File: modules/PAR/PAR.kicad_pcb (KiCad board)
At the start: 2 copper layers, 160 x 100 mm, 30 parts, among them J1 CardConnector, SW1 SW_DIP_x06, U1 2102, U10 74AHCT541, U11 74HCT32, U12 74AHCT244, U13 74HCT00, U14 74HC688, U15 74AHCT244, U2 2102, U3 2102, U4 2102, U5 2102, U6 2102, U7 2102, U8 2102, U9 74AHCT541

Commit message: serial & cpu card
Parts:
- removed C1, C10, C11, C2, C3, C4, C5, C6, C7, C8: 100n, IMNOTWOPR:C_Rect_P200mil
- removed C9: 47u, IMNOTWOPR:CP_Radial_Tantal_P100mil
- removed RN1: 10k, Resistor_THT:R_Array_SIP7
- removed SW1: SW_DIP_x06, Button_Switch_THT:SW_DIP_SPSTx06_Slide_9.78x17.42mm_W7.62mm_P2.54mm
- removed U1, U2, U3, U4, U5, U6, U7, U8: 2102, IMNOTWOPR:DIP-16N
- removed U10, U9: 74AHCT541, IMNOTWOPR:DIP-20N
- removed U11: 74HCT32, IMNOTWOPR:DIP-14N
- removed U12, U15: 74AHCT244, IMNOTWOPR:DIP-20N
- removed U13: 74HCT00, IMNOTWOPR:DIP-14N
- removed U14: 74HC688, IMNOTWOPR:DIP-20N
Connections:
- J1 pad a10: /RAM-1/SA6 -> /TEMPLATE/S6
- J1 pad a11: /RAM-1/SA7 -> /TEMPLATE/S7
- J1 pad a12: /RAM-1/SA8 -> /TEMPLATE/S8
- J1 pad a13: /RAM-1/SA9 -> /TEMPLATE/S9
- J1 pad a14: /RAM-1/SA10 -> /TEMPLATE/S10
- J1 pad a15: /RAM-1/SA11 -> /TEMPLATE/S11
- J1 pad a16: /RAM-1/SA12 -> /TEMPLATE/S12
- J1 pad a17: /RAM-1/SA13 -> /TEMPLATE/S13
- J1 pad a18: /RAM-1/SA14 -> /TEMPLATE/S14
- J1 pad a19: /RAM-1/SA15 -> /TEMPLATE/S15
- J1 pad a4: /RAM-1/SA0 -> /TEMPLATE/S0
- J1 pad a5: /RAM-1/SA1 -> /TEMPLATE/S1
- J1 pad a6: /RAM-1/SA2 -> /TEMPLATE/S2
- J1 pad a7: /RAM-1/SA3 -> /TEMPLATE/S3
- J1 pad a8: /RAM-1/SA4 -> /TEMPLATE/S4
- J1 pad a9: /RAM-1/SA5 -> /TEMPLATE/S5
- J1 pad b10: /RAM-1/SD6 -> unconnected-(J1B-D_{6}-Padb10)
- J1 pad b11: /RAM-1/SD7 -> unconnected-(J1B-D_{7}-Padb11)
- J1 pad b12: /RAM-1/PHI2 -> unconnected-(J1B-Φ_{2}-Padb12)
- J1 pad b13: /RAM-1/R~{W} -> unconnected-(J1B-R~{W}-Padb13)
- J1 pad b4: /RAM-1/SD0 -> unconnected-(J1B-D_{0}-Padb4)
- J1 pad b5: /RAM-1/SD1 -> unconnected-(J1B-D_{1}-Padb5)
- J1 pad b6: /RAM-1/SD2 -> unconnected-(J1B-D_{2}-Padb6)
- J1 pad b7: /RAM-1/SD3 -> unconnected-(J1B-D_{3}-Padb7)
- J1 pad b8: /RAM-1/SD4 -> unconnected-(J1B-D_{4}-Padb8)
- J1 pad b9: /RAM-1/SD5 -> unconnected-(J1B-D_{5}-Padb9)
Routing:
- net GND: track 200.7 -> 0.00 mm
- net +5V: track 106.8 -> 0.00 mm, vias 1 -> 0
- net /RAM-1/A12: track 86.9 -> 0.00 mm
- net /RAM-1/A11: track 84.3 -> 0.00 mm
- net /RAM-1/A10: track 81.8 -> 0.00 mm
- net /RAM-1/A5: track 81.4 -> 0.00 mm
- net /RAM-1/A6: track 81.4 -> 0.00 mm
- net /RAM-1/A1: track 81.4 -> 0.00 mm
- net /RAM-1/A7: track 81.4 -> 0.00 mm
- net /RAM-1/A9: track 81.4 -> 0.00 mm
- net /RAM-1/A8: track 81.4 -> 0.00 mm
- net /RAM-1/A4: track 81.4 -> 0.00 mm
- net /RAM-1/A3: track 81.4 -> 0.00 mm
- net /RAM-1/A2: track 81.4 -> 0.00 mm
- net /RAM-1/A0: track 81.4 -> 0.00 mm
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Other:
- board text removed: "Mounting holes are optional Keepout areas are for for guide rails"

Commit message: par board & schematic wip
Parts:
- added C1: 47µ, IMNOTWOPR:CP_Radial_Tantal_P100mil, F.Cu at (189.4, 48.6)
- added C10: 100n, IMNOTWOPR:C_Rect_P200mil, F.Cu at (184.3, 53.1)
- added C2: 100n, IMNOTWOPR:C_Rect_P200mil, F.Cu at (157.6, 139.4)
- added C3: 100n, IMNOTWOPR:C_Rect_P200mil, F.Cu at (129.7, 139.4)
- added C4: 100n, IMNOTWOPR:C_Rect_P200mil, F.Cu at (197.0, 53.1)
- added C5: 100n, IMNOTWOPR:C_Rect_P200mil, F.Cu at (197.0, 81.0)
- added C6: 100n, IMNOTWOPR:C_Rect_P200mil, F.Cu at (184.3, 101.3)
- added C7: 100n, IMNOTWOPR:C_Rect_P200mil, F.Cu at (184.3, 73.4)
- added C8: 100n, IMNOTWOPR:C_Rect_P200mil, F.Cu at (147.5, 63.2)
- added C9: 100n, IMNOTWOPR:C_Rect_P200mil, F.Cu at (132.2, 65.8)
- added D1: SB140, Diode_THT:D_DO-41_SOD81_P10.16mm_Horizontal, F.Cu at (181.8, 132.7)
- added D2: SB140, Diode_THT:D_DO-41_SOD81_P10.16mm_Horizontal, F.Cu at (181.8, 136.9)
- added JP1: PORT1A, IMNOTWOPR:Jumper_1x03, F.Cu at (109.4, 51.8)
- added JP2: PORT2A, IMNOTWOPR:Jumper_1x03, F.Cu at (109.4, 100.1)
- added JP3: PORT2B, IMNOTWOPR:Jumper_1x03, F.Cu at (109.4, 133.1)
- added JP4: PORT1B, IMNOTWOPR:Jumper_1x03, F.Cu at (109.4, 84.8)
- added R1: 100R, Resistor_THT:R_Axial_DIN0207_L6.3mm_D2.5mm_P2.54mm_Vertical, F.Cu at (101.8, 60.7)
- added R10: 100R, Resistor_THT:R_Axial_DIN0207_L6.3mm_D2.5mm_P2.54mm_Vertical, F.Cu at (78.9, 58.2)
- added R11: 100R, Resistor_THT:R_Axial_DIN0207_L6.3mm_D2.5mm_P2.54mm_Vertical, F.Cu at (101.8, 109.0)
- added R12: 100R, Resistor_THT:R_Axial_DIN0207_L6.3mm_D2.5mm_P2.54mm_Vertical, F.Cu at (99.2, 106.4)
- added R13: 100R, Resistor_THT:R_Axial_DIN0207_L6.3mm_D2.5mm_P2.54mm_Vertical, F.Cu at (96.7, 109.0)
- added R14: 100R, Resistor_THT:R_Axial_DIN0207_L6.3mm_D2.5mm_P2.54mm_Vertical, F.Cu at (94.1, 106.4)
- added R15: 100R, Resistor_THT:R_Axial_DIN0207_L6.3mm_D2.5mm_P2.54mm_Vertical, F.Cu at (91.6, 109.0)
- added R16: 100R, Resistor_THT:R_Axial_DIN0207_L6.3mm_D2.5mm_P2.54mm_Vertical, F.Cu at (89.0, 106.4)
- added R17: 100R, Resistor_THT:R_Axial_DIN0207_L6.3mm_D2.5mm_P2.54mm_Vertical, F.Cu at (86.5, 109.0)
- added R18: 100R, Resistor_THT:R_Axial_DIN0207_L6.3mm_D2.5mm_P2.54mm_Vertical, F.Cu at (84.0, 106.4)
- added R19: 100R, Resistor_THT:R_Axial_DIN0207_L6.3mm_D2.5mm_P2.54mm_Vertical, F.Cu at (81.4, 109.0)
- added R2: 100R, Resistor_THT:R_Axial_DIN0207_L6.3mm_D2.5mm_P2.54mm_Vertical, F.Cu at (99.2, 58.2)
- added R20: 100R, Resistor_THT:R_Axial_DIN0207_L6.3mm_D2.5mm_P2.54mm_Vertical, F.Cu at (78.9, 106.4)
- added R21: 100R, Resistor_THT:R_Axial_DIN0207_L6.3mm_D2.5mm_P2.54mm_Vertical, F.Cu at (101.8, 129.3)
- added R22: 100R, Resistor_THT:R_Axial_DIN0207_L6.3mm_D2.5mm_P2.54mm_Vertical, F.Cu at (99.2, 131.8)
- added R23: 100R, Resistor_THT:R_Axial_DIN0207_L6.3mm_D2.5mm_P2.54mm_Vertical, F.Cu at (96.7, 129.3)
- added R24: 100R, Resistor_THT:R_Axial_DIN0207_L6.3mm_D2.5mm_P2.54mm_Vertical, F.Cu at (94.1, 131.8)
- added R25: 100R, Resistor_THT:R_Axial_DIN0207_L6.3mm_D2.5mm_P2.54mm_Vertical, F.Cu at (91.6, 129.3)
- added R26: 100R, Resistor_THT:R_Axial_DIN0207_L6.3mm_D2.5mm_P2.54mm_Vertical, F.Cu at (89.0, 131.8)
- added R27: 100R, Resistor_THT:R_Axial_DIN0207_L6.3mm_D2.5mm_P2.54mm_Vertical, F.Cu at (86.5, 129.3)
- added R28: 100R, Resistor_THT:R_Axial_DIN0207_L6.3mm_D2.5mm_P2.54mm_Vertical, F.Cu at (84.0, 131.8)
- added R29: 100R, Resistor_THT:R_Axial_DIN0207_L6.3mm_D2.5mm_P2.54mm_Vertical, F.Cu at (81.4, 129.3)
- added R3: 100R, Resistor_THT:R_Axial_DIN0207_L6.3mm_D2.5mm_P2.54mm_Vertical, F.Cu at (96.7, 60.7)
- added R30: 100R, Resistor_THT:R_Axial_DIN0207_L6.3mm_D2.5mm_P2.54mm_Vertical, F.Cu at (78.9, 131.8)
- added R31: 100R, Resistor_THT:R_Axial_DIN0207_L6.3mm_D2.5mm_P2.54mm_Vertical, F.Cu at (101.8, 81.0)
- added R32: 100R, Resistor_THT:R_Axial_DIN0207_L6.3mm_D2.5mm_P2.54mm_Vertical, F.Cu at (99.2, 83.6)
- added R33: 100R, Resistor_THT:R_Axial_DIN0207_L6.3mm_D2.5mm_P2.54mm_Vertical, F.Cu at (96.7, 81.0)
- added R34: 100R, Resistor_THT:R_Axial_DIN0207_L6.3mm_D2.5mm_P2.54mm_Vertical, F.Cu at (94.1, 83.6)
- added R35: 100R, Resistor_THT:R_Axial_DIN0207_L6.3mm_D2.5mm_P2.54mm_Vertical, F.Cu at (91.6, 81.0)
- added R36: 100R, Resistor_THT:R_Axial_DIN0207_L6.3mm_D2.5mm_P2.54mm_Vertical, F.Cu at (89.0, 83.6)
- added R37: 100R, Resistor_THT:R_Axial_DIN0207_L6.3mm_D2.5mm_P2.54mm_Vertical, F.Cu at (86.5, 81.0)
- added R38: 100R, Resistor_THT:R_Axial_DIN0207_L6.3mm_D2.5mm_P2.54mm_Vertical, F.Cu at (84.0, 83.6)
- added R39: 100R, Resistor_THT:R_Axial_DIN0207_L6.3mm_D2.5mm_P2.54mm_Vertical, F.Cu at (81.4, 81.0)
- added R4: 100R, Resistor_THT:R_Axial_DIN0207_L6.3mm_D2.5mm_P2.54mm_Vertical, F.Cu at (94.1, 58.2)
- added R40: 100R, Resistor_THT:R_Axial_DIN0207_L6.3mm_D2.5mm_P2.54mm_Vertical, F.Cu at (78.9, 83.6)
- added R5: 100R, Resistor_THT:R_Axial_DIN0207_L6.3mm_D2.5mm_P2.54mm_Vertical, F.Cu at (91.6, 60.7)
- added R6: 100R, Resistor_THT:R_Axial_DIN0207_L6.3mm_D2.5mm_P2.54mm_Vertical, F.Cu at (89.0, 58.2)
- added R7: 100R, Resistor_THT:R_Axial_DIN0207_L6.3mm_D2.5mm_P2.54mm_Vertical, F.Cu at (86.5, 60.7)
- added R8: 100R, Resistor_THT:R_Axial_DIN0207_L6.3mm_D2.5mm_P2.54mm_Vertical, F.Cu at (84.0, 58.2)
- added R9: 100R, Resistor_THT:R_Axial_DIN0207_L6.3mm_D2.5mm_P2.54mm_Vertical, F.Cu at (81.4, 60.7)
- added RN1: 10k, Resistor_THT:R_Array_SIP9, F.Cu at (170.3, 60.7)
- added RN2: 10k, Resistor_THT:R_Array_SIP11, F.Cu at (104.3, 54.4)
- added RN3: 10k, Resistor_THT:R_Array_SIP11, F.Cu at (104.3, 102.6)
- added RN4: 10k, Resistor_THT:R_Array_SIP11, F.Cu at (104.3, 135.6)
- added RN5: 10k, Resistor_THT:R_Array_SIP11, F.Cu at (104.3, 87.4)
- added SW1: SW_DIP_x08, Button_Switch_THT:SW_DIP_SPSTx08_Slide_9.78x22.5mm_W7.62mm_P2.54mm, F.Cu at (158.9, 63.2)
- added U1: W65C22, IMNOTWOPR:DIP-40W, F.Cu at (162.7, 112.8)
- added U10: DB-25 VIA, IMNOTWOPR:IDC-Header_2x13_DB-25, F.Cu at (101.8, 69.6)
- added U11: DB-25 VIA, IMNOTWOPR:IDC-Header_2x13_DB-25, F.Cu at (101.8, 117.9)
- added U2: 74HCT30, IMNOTWOPR:DIP-14N, F.Cu at (131.0, 76.0)
- added U3: 74HCT00, IMNOTWOPR:DIP-14N, F.Cu at (183.0, 63.2)
- added U4: 74AHCT541, IMNOTWOPR:DIP-20N, F.Cu at (195.7, 67.1)
- added U5: 74AHCT541, IMNOTWOPR:DIP-20N, F.Cu at (195.7, 95.0)
- added U6: W65C22, IMNOTWOPR:DIP-40W, F.Cu at (134.8, 112.8)
- added U7: 74AHCT245, IMNOTWOPR:DIP-20N, F.Cu at (183.0, 115.3)
- added U8: 74HCT688, IMNOTWOPR:DIP-20N, F.Cu at (183.0, 87.4)
- added U9: 74HCT138, IMNOTWOPR:DIP-16N, F.Cu at (146.2, 74.7)
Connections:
- J1 pad a10: /TEMPLATE/S6 -> Net-(J1A-A_{6})
- J1 pad a11: /TEMPLATE/S7 -> Net-(J1A-A_{7})
- J1 pad a12: /TEMPLATE/S8 -> Net-(J1A-A_{8})
- J1 pad a13: /TEMPLATE/S9 -> Net-(J1A-A_{9})
- J1 pad a14: /TEMPLATE/S10 -> Net-(J1A-A_{10})
- J1 pad a15: /TEMPLATE/S11 -> Net-(J1A-A_{11})
- J1 pad a16: /TEMPLATE/S12 -> Net-(J1A-A_{12})
- J1 pad a17: /TEMPLATE/S13 -> Net-(J1A-A_{13})
- J1 pad a18: /TEMPLATE/S14 -> Net-(J1A-A_{14})
- J1 pad a19: /TEMPLATE/S15 -> Net-(J1A-A_{15})
- J1 pad a4: /TEMPLATE/S0 -> Net-(J1A-A_{0})
- J1 pad a5: /TEMPLATE/S1 -> Net-(J1A-A_{1})
- J1 pad a6: /TEMPLATE/S2 -> Net-(J1A-A_{2})
- J1 pad a7: /TEMPLATE/S3 -> Net-(J1A-A_{3})
- J1 pad a8: /TEMPLATE/S4 -> Net-(J1A-A_{4})
- J1 pad a9: /TEMPLATE/S5 -> Net-(J1A-A_{5})
- J1 pad b22: unconnected-(J1B-~{BUS_ACK}-Padb22) -> Net-(J1B-D_{0})
- J1 pad b23: unconnected-(J1B-~{ABORT}-Padb23) -> Net-(J1B-D_{1})
- J1 pad b24: unconnected-(J1B-SYNC-Padb24) -> Net-(J1B-D_{2})
- J1 pad b25: unconnected-(J1B-VPB-Padb25) -> Net-(J1B-D_{3})
- J1 pad b26: unconnected-(J1B-MLB-Padb26) -> Net-(J1B-D_{4})
- J1 pad b27: unconnected-(J1B-VDA-Padb27) -> Net-(J1B-D_{5})
- J1 pad b28: unconnected-(J1B-VPA-Padb28) -> Net-(J1B-D_{6})
- J1 pad b29: unconnected-(J1B-RESERVED-Padb29) -> Net-(J1B-D_{7})
- J1 pad b4: unconnected-(J1B-D_{0}-Padb4) -> /#VALID
- J1 pad b5: unconnected-(J1B-D_{1}-Padb5) -> /PHI2
- J1 pad b6: unconnected-(J1B-D_{2}-Padb6) -> /R/W
- J1 pad b7: unconnected-(J1B-D_{3}-Padb7) -> /#RESET
- J1 pad b8: unconnected-(J1B-D_{4}-Padb8) -> /#IRQ
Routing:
- net GND: track 0.00 -> 500.6 mm, vias 0 -> 3
- net +5V: track 0.00 -> 427.3 mm, vias 0 -> 4
- net /PORT1_PB7: track 0.00 -> 114.8 mm, vias 0 -> 2
- net /PORT1_PB6: track 0.00 -> 108.5 mm, vias 0 -> 2
- net /PORT1_PA7: track 0.00 -> 102.1 mm, vias 0 -> 2
- net /PORT1_PB5: track 0.00 -> 102.1 mm, vias 0 -> 2
- net /PORT1_PA6: track 0.00 -> 97.0 mm, vias 0 -> 2
- net /PORT1_PB4: track 0.00 -> 95.8 mm, vias 0 -> 2
- net /PORT1_PA5: track 0.00 -> 92.0 mm, vias 0 -> 2
- net /A1: track 0.00 -> 90.3 mm
- net /A2: track 0.00 -> 90.3 mm
- net /PORT1_PB3: track 0.00 -> 89.4 mm, vias 0 -> 2
- net /PORT1_CB2: track 0.00 -> 89.4 mm, vias 0 -> 2
- net /PORT1_PA4: track 0.00 -> 86.9 mm, vias 0 -> 2
- net /PORT1_CB1: track 0.00 -> 83.1 mm, vias 0 -> 2
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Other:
- board text removed: "${TITLE}"

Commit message: bus overhaul and par wip
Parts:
- moved R19 104.2 mm to (-22.7, 58.2)
- moved R29 104.2 mm to (-22.7, 126.8)
- moved R39 104.2 mm to (-22.7, 78.5)
- moved R9 104.2 mm to (-22.7, 106.4)
- moved U1 104.2 mm to (58.6, 110.2)
- moved U2 104.2 mm to (30.6, 110.2)
- moved C1 104.2 mm to (85.2, 46.1)
- moved C3 104.2 mm to (25.6, 136.9)
- moved JP1 104.2 mm to (5.23, 97.5)
- moved JP2 104.2 mm to (5.23, 49.3)
- moved JP3 104.2 mm to (5.23, 130.6)
- moved JP4 104.2 mm to (5.23, 82.3)
- moved R1 104.2 mm to (-2.39, 106.4)
- moved R10 104.2 mm to (-25.2, 103.9)
- moved R11 104.2 mm to (-2.39, 58.2)
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- renumbered JP2 to JP1, JP1 to JP2, R11 to R1, R20 to R10, R1 to R11, R2 to R12, R3 to R13, R4 to R14, R5 to R15, R6 to R16, R7 to R17, R8 to R18, R9 to R19, R12 to R2, R10 to R20, R13 to R3, R14 to R4, R15 to R5, R16 to R6, R17 to R7, R18 to R8, R19 to R9, RN3 to RN2, RN2 to RN3, U11 to U10, U10 to U11, U6 to U2, U2 to U3, U3 to U4, U4 to U5, U5 to U6
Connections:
- J1 pad a10: Net-(J1A-A_{6}) -> Net-(J1A-A_{14})
- J1 pad a11: Net-(J1A-A_{7}) -> Net-(J1A-A_{15})
- J1 pad a12: Net-(J1A-A_{8}) -> unconnected-(J1A-A_{16}-Pada12)
- J1 pad a13: Net-(J1A-A_{9}) -> unconnected-(J1A-A_{17}-Pada13)
- J1 pad a14: Net-(J1A-A_{10}) -> unconnected-(J1A-A_{18}-Pada14)
- J1 pad a15: Net-(J1A-A_{11}) -> unconnected-(J1A-A_{19}-Pada15)
- J1 pad a16: Net-(J1A-A_{12}) -> unconnected-(J1A-A_{20}-Pada16)
- J1 pad a17: Net-(J1A-A_{13}) -> unconnected-(J1A-A_{21}-Pada17)
- J1 pad a18: Net-(J1A-A_{14}) -> unconnected-(J1A-A_{22}-Pada18)
- J1 pad a19: Net-(J1A-A_{15}) -> unconnected-(J1A-A_{23}-Pada19)
- J1 pad a4: Net-(J1A-A_{0}) -> Net-(J1A-A_{8})
- J1 pad a5: Net-(J1A-A_{1}) -> Net-(J1A-A_{9})
- J1 pad a6: Net-(J1A-A_{2}) -> Net-(J1A-A_{10})
- J1 pad a7: Net-(J1A-A_{3}) -> Net-(J1A-A_{11})
- J1 pad a8: Net-(J1A-A_{4}) -> Net-(J1A-A_{12})
- J1 pad a9: Net-(J1A-A_{5}) -> Net-(J1A-A_{13})
- J1 pad b10: unconnected-(J1B-READY-Padb10) -> Net-(J1B-A_{6})
- J1 pad b11: unconnected-(J1B-BE-Padb11) -> Net-(J1B-A_{7})
- J1 pad b12: unconnected-(J1B-SYNC-Padb12) -> /#RESET
- J1 pad b13: unconnected-(J1B-VPB-Padb13) -> /PHI2
- J1 pad b14: unconnected-(J1B-MLB-Padb14) -> /R/W
- J1 pad b15: unconnected-(J1B-VDA-Padb15) -> /#VALID
- J1 pad b16: unconnected-(J1B-VPA-Padb16) -> Net-(J1B-D_{0})
- J1 pad b17: unconnected-(J1B-E-Padb17) -> Net-(J1B-D_{1})
- J1 pad b18: unconnected-(J1B-MX-Padb18) -> Net-(J1B-D_{2})
- J1 pad b19: unconnected-(J1B-~{BANK0}-Padb19) -> Net-(J1B-D_{3})
- J1 pad b20: unconnected-(J1B-~{BANK1}-Padb20) -> Net-(J1B-D_{4})
- J1 pad b21: unconnected-(J1B-~{BANK2}-Padb21) -> Net-(J1B-D_{5})
- J1 pad b22: Net-(J1B-D_{0}) -> Net-(J1B-D_{6})
- J1 pad b23: Net-(J1B-D_{1}) -> Net-(J1B-D_{7})
- J1 pad b24: Net-(J1B-D_{2}) -> /#IRQ
- J1 pad b25: Net-(J1B-D_{3}) -> unconnected-(J1B-NMI-Padb25)
- J1 pad b26: Net-(J1B-D_{4}) -> unconnected-(J1B-IRQ_{0}-Padb26)
- J1 pad b27: Net-(J1B-D_{5}) -> unconnected-(J1B-IRQ_{1}-Padb27)
- J1 pad b28: Net-(J1B-D_{6}) -> unconnected-(J1B-IRQ_{2}-Padb28)
- J1 pad b29: Net-(J1B-D_{7}) -> unconnected-(J1B-IRQ_{3}-Padb29)
- J1 pad b4: /#VALID -> Net-(J1B-A_{0})
- J1 pad b5: /PHI2 -> Net-(J1B-A_{1})
- J1 pad b6: /R/W -> Net-(J1B-A_{2})
- J1 pad b7: /#RESET -> Net-(J1B-A_{3})
- J1 pad b8: /#IRQ -> Net-(J1B-A_{4})
- J1 pad b9: unconnected-(J1B-NMI-Padb9) -> Net-(J1B-A_{5})
- U5 pad 2: Net-(J1A-A_{0}) -> Net-(J1B-A_{0})
- U5 pad 3: Net-(J1A-A_{1}) -> Net-(J1B-A_{1})
- U5 pad 4: Net-(J1A-A_{2}) -> Net-(J1B-A_{2})
- U5 pad 5: Net-(J1A-A_{3}) -> Net-(J1B-A_{3})
- U5 pad 6: Net-(J1A-A_{4}) -> Net-(J1B-A_{4})
- U5 pad 7: Net-(J1A-A_{5}) -> Net-(J1B-A_{5})
- U5 pad 8: Net-(J1A-A_{6}) -> Net-(J1B-A_{6})
- U5 pad 9: Net-(J1A-A_{7}) -> Net-(J1B-A_{7})
- U9 pad 4: GND -> /#PAGE_SELECT
- U9 pad 5: /#PAGE_SELECT -> GND
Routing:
- net GND: track 500.6 -> 52.6 mm, vias 3 -> 0
- net +5V: track 427.3 -> 62.8 mm, vias 4 -> 0
- net /PORT1_PB7: track 114.8 -> 0.00 mm, vias 2 -> 0
- net /PORT1_PB6: track 108.5 -> 0.00 mm, vias 2 -> 0
- net /PORT1_PA7: track 102.1 -> 0.00 mm, vias 2 -> 0
- net /PORT1_PB5: track 102.1 -> 0.00 mm, vias 2 -> 0
- net /PORT1_PA6: track 97.0 -> 0.00 mm, vias 2 -> 0
- net /PORT1_PB4: track 95.8 -> 0.00 mm, vias 2 -> 0
- net /PORT1_PA5: track 92.0 -> 0.00 mm, vias 2 -> 0
- net /PORT1_PB3: track 89.4 -> 0.00 mm, vias 2 -> 0
- net /PORT1_CB2: track 89.4 -> 0.00 mm, vias 2 -> 0
- net /PORT1_PA4: track 86.9 -> 0.00 mm, vias 2 -> 0
- net /PORT1_CB1: track 83.1 -> 0.00 mm, vias 2 -> 0
- net /PORT1_PB2: track 83.1 -> 0.00 mm, vias 2 -> 0
- net /PORT1_PA3: track 81.8 -> 0.00 mm, vias 2 -> 0
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
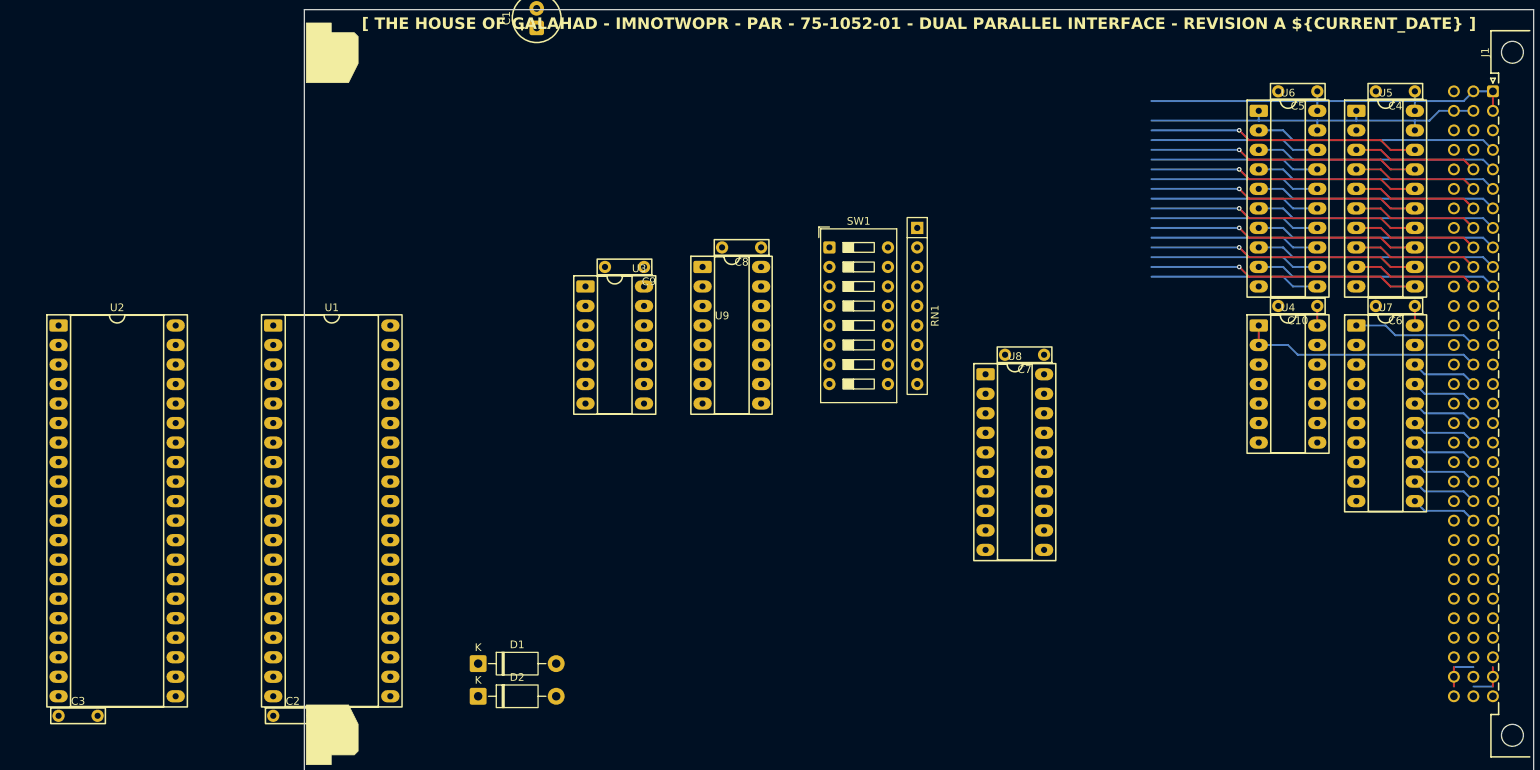
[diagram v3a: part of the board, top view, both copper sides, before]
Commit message: added monitor and clk pcb
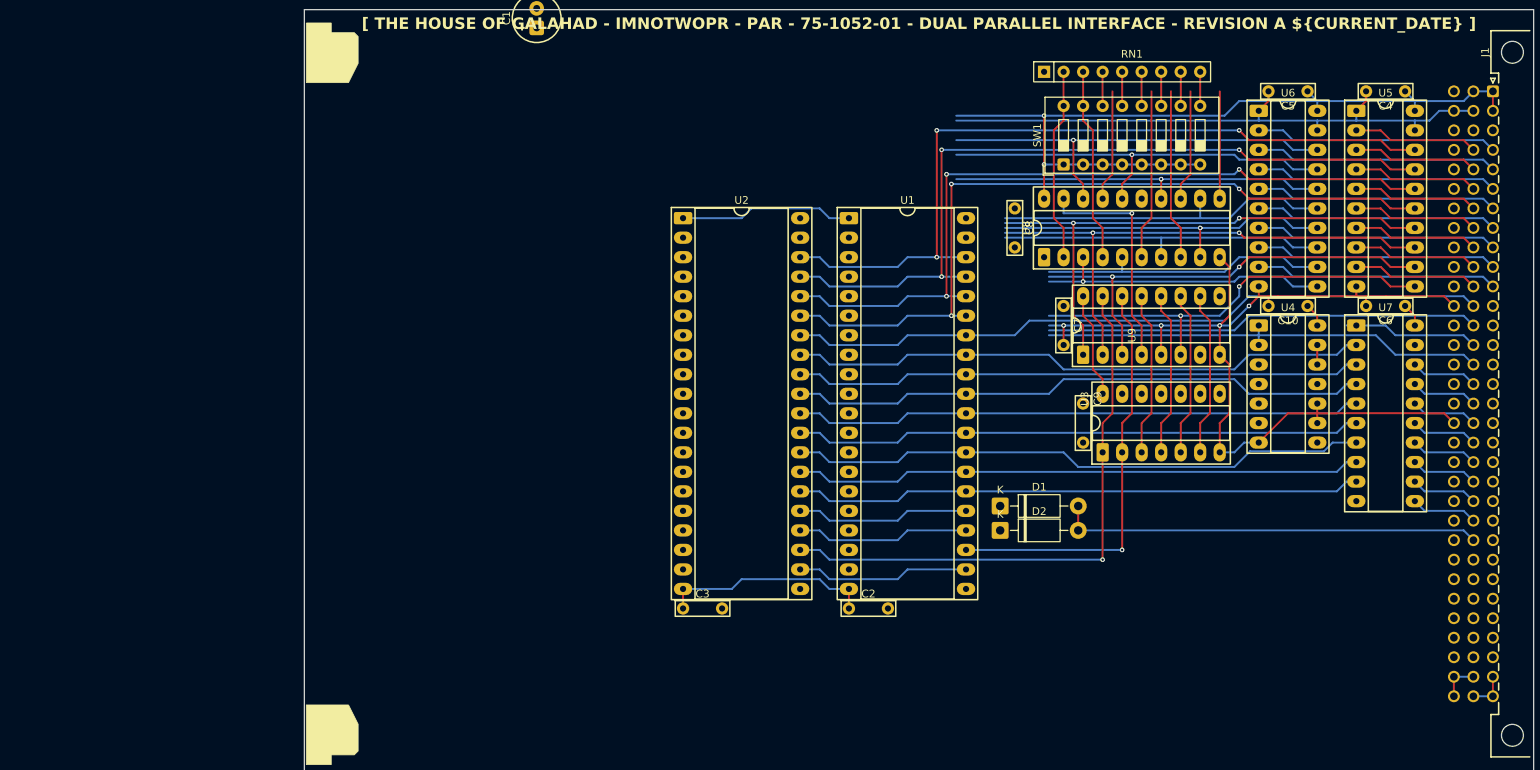
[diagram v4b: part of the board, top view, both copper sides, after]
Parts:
- moved C3 82.5 mm to (106.8, 122.9)
- moved U2 82.5 mm to (111.9, 96.3)
- moved U1 76.2 mm to (133.5, 96.3)
- moved C2 76.2 mm to (128.4, 122.9)
- moved U3 71.8 mm to (166.5, 98.8), turned to 90 degrees
- moved D2 71.3 mm to (145.6, 112.8)
- moved D1 71.0 mm to (145.6, 109.6)
- moved C9 63.1 mm to (156.4, 98.8), turned to -90 degrees
- moved U9 54.6 mm to (165.2, 86.1), turned to 90 degrees
- moved C8 35.7 mm to (147.5, 73.4), turned to -90 degrees
- moved U8 34.1 mm to (162.7, 73.4), turned to 90 degrees
- moved SW1 32.3 mm to (153.8, 65.2), turned to 90 degrees
- moved RN1 26.2 mm to (151.3, 53.1), turned to 0 degrees
- moved C7 6.35 mm to (153.8, 86.1), turned to -90 degrees
- moved C10 1.27 mm to (183.0, 83.6)
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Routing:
- net GND: track 52.6 -> 238.7 mm, vias 0 -> 4
- net +5V: track 62.8 -> 186.3 mm, vias 0 -> 2
- net /#RESET: track 0.00 -> 90.0 mm
- net /PHI2: track 0.00 -> 79.2 mm
- net /D5: track 0.00 -> 75.5 mm
- net /D2: track 0.00 -> 75.5 mm
- net /D0: track 0.00 -> 75.5 mm
- net /#VIA_1_CS: track 0.00 -> 75.2 mm, vias 0 -> 1
- net /D7: track 0.00 -> 74.0 mm
- net /D6: track 0.00 -> 74.0 mm
- net /D3: track 0.00 -> 74.0 mm
- net /D1: track 0.00 -> 74.0 mm
- net /D4: track 0.00 -> 74.0 mm
- net /A0: track 35.3 -> 102.4 mm, vias 1 -> 3
- net /A1: track 35.3 -> 101.8 mm, vias 1 -> 3
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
